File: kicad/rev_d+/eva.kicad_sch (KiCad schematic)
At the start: 0 parts

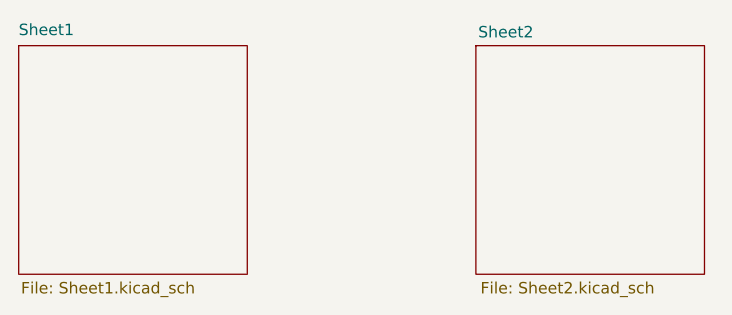
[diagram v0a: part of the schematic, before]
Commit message: pentevo: rev D+: add I2C ext. connector, update HDMI mezzanine board connector with analog power and I2C
git-svn-id: svn://localhost/local-pentevo@1353 c6c76956-fad2-4150-a3a9-ea0a427205ba
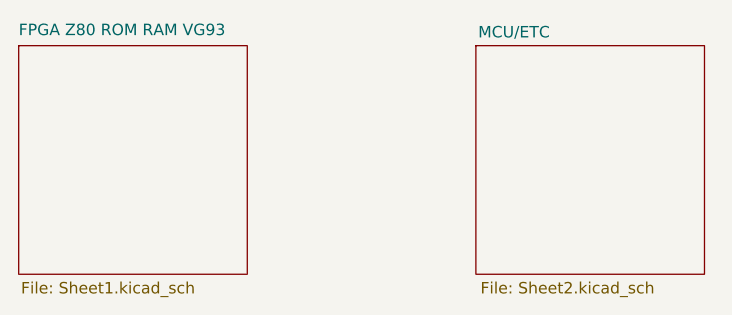
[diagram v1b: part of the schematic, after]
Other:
- sheet Sheet1 renamed FPGA Z80 ROM RAM VG93
- sheet Sheet2 renamed MCU/ETC
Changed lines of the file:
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@@
 			(color 128 255 128 1.0000)
 		)
-		(property "Sheetname" "Sheet2"
+		(property "Sheetname" "MCU/ETC"
 			(at 76.454 75.438 0)
 			(effects
@@
 			(color 128 255 128 1.0000)
 		)
-		(property "Sheetname" "Sheet1"
+		(property "Sheetname" "FPGA Z80 ROM RAM VG93"
 			(at 25.4 75.184 0)
 			(effects
